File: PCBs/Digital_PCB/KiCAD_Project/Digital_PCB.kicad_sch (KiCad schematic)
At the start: 46 parts, among them J1 NP_Conn_01x02_Relief, J2 Board to Board, J3 NP_Conn_01x04_Relief, J4 1-0001205, J5 NP_Conn_01x04, J6 NP_Conn_01x02_Relief, J7 NP_Conn_01x04, U1 1-0000207, Y1 1-0000721

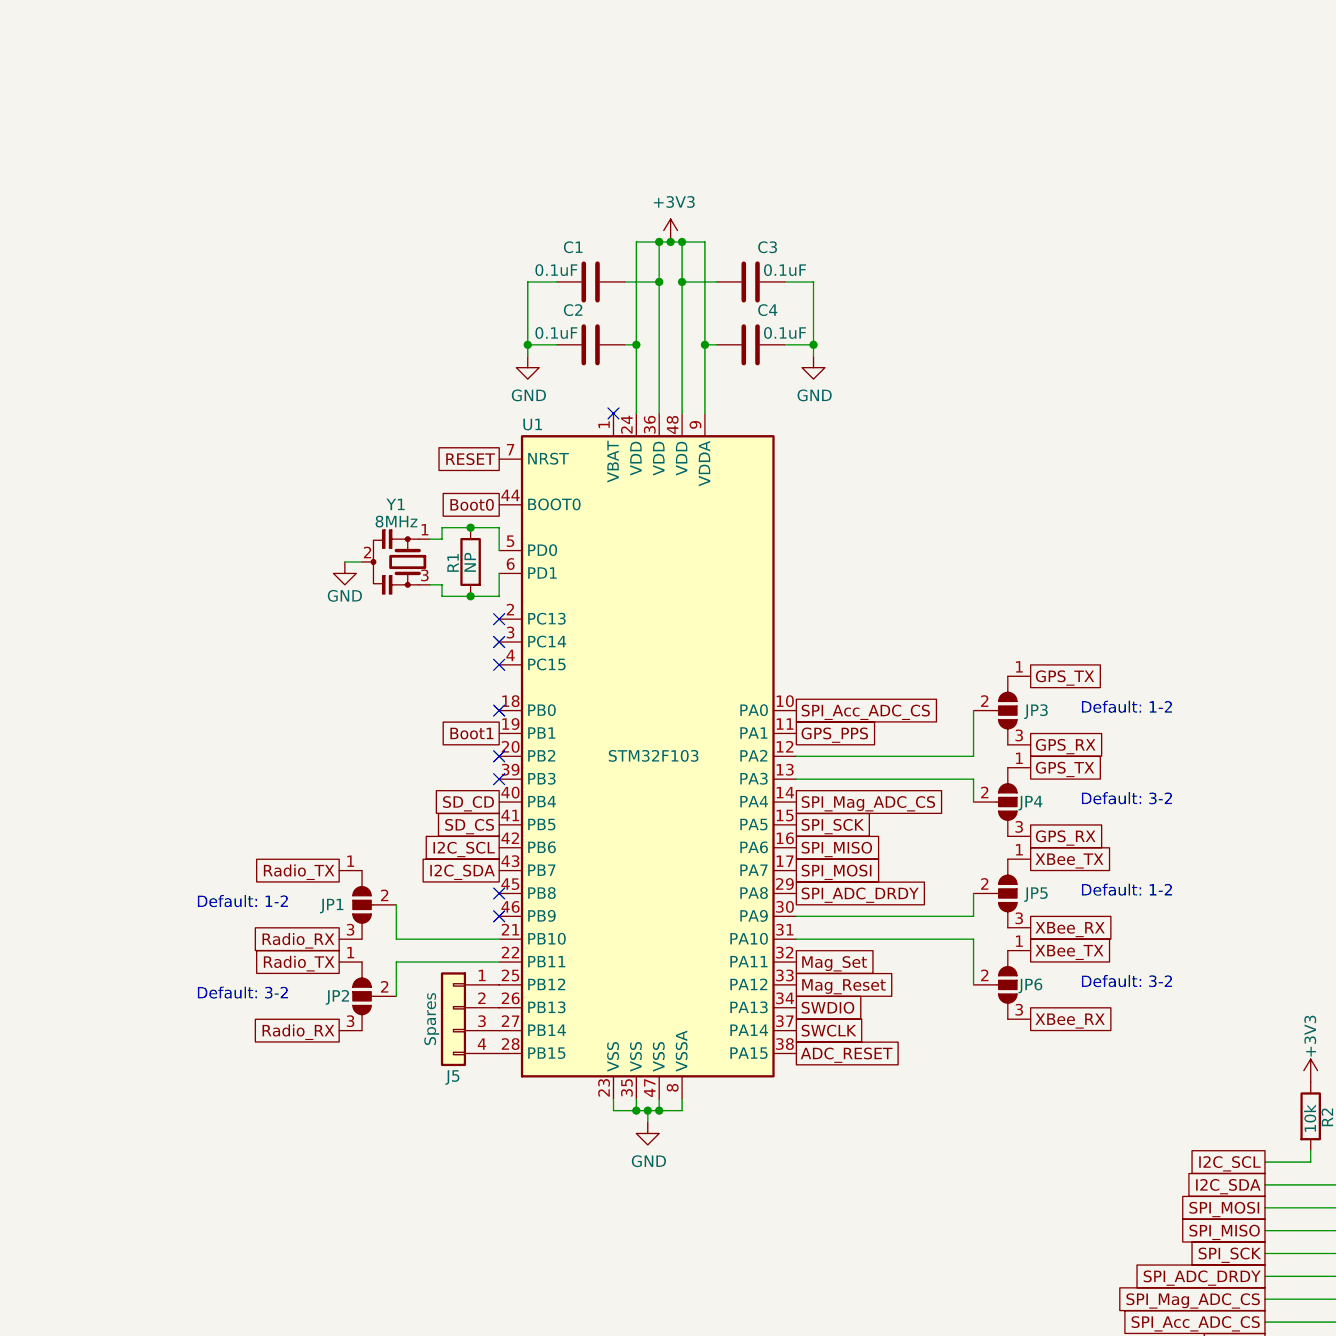
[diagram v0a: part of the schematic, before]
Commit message: Digital PCB Revisions: Fixed ERC Footprint/Symbol Errors Fixed Remaining ERC Errors Relocated U7 to bottom of PCB
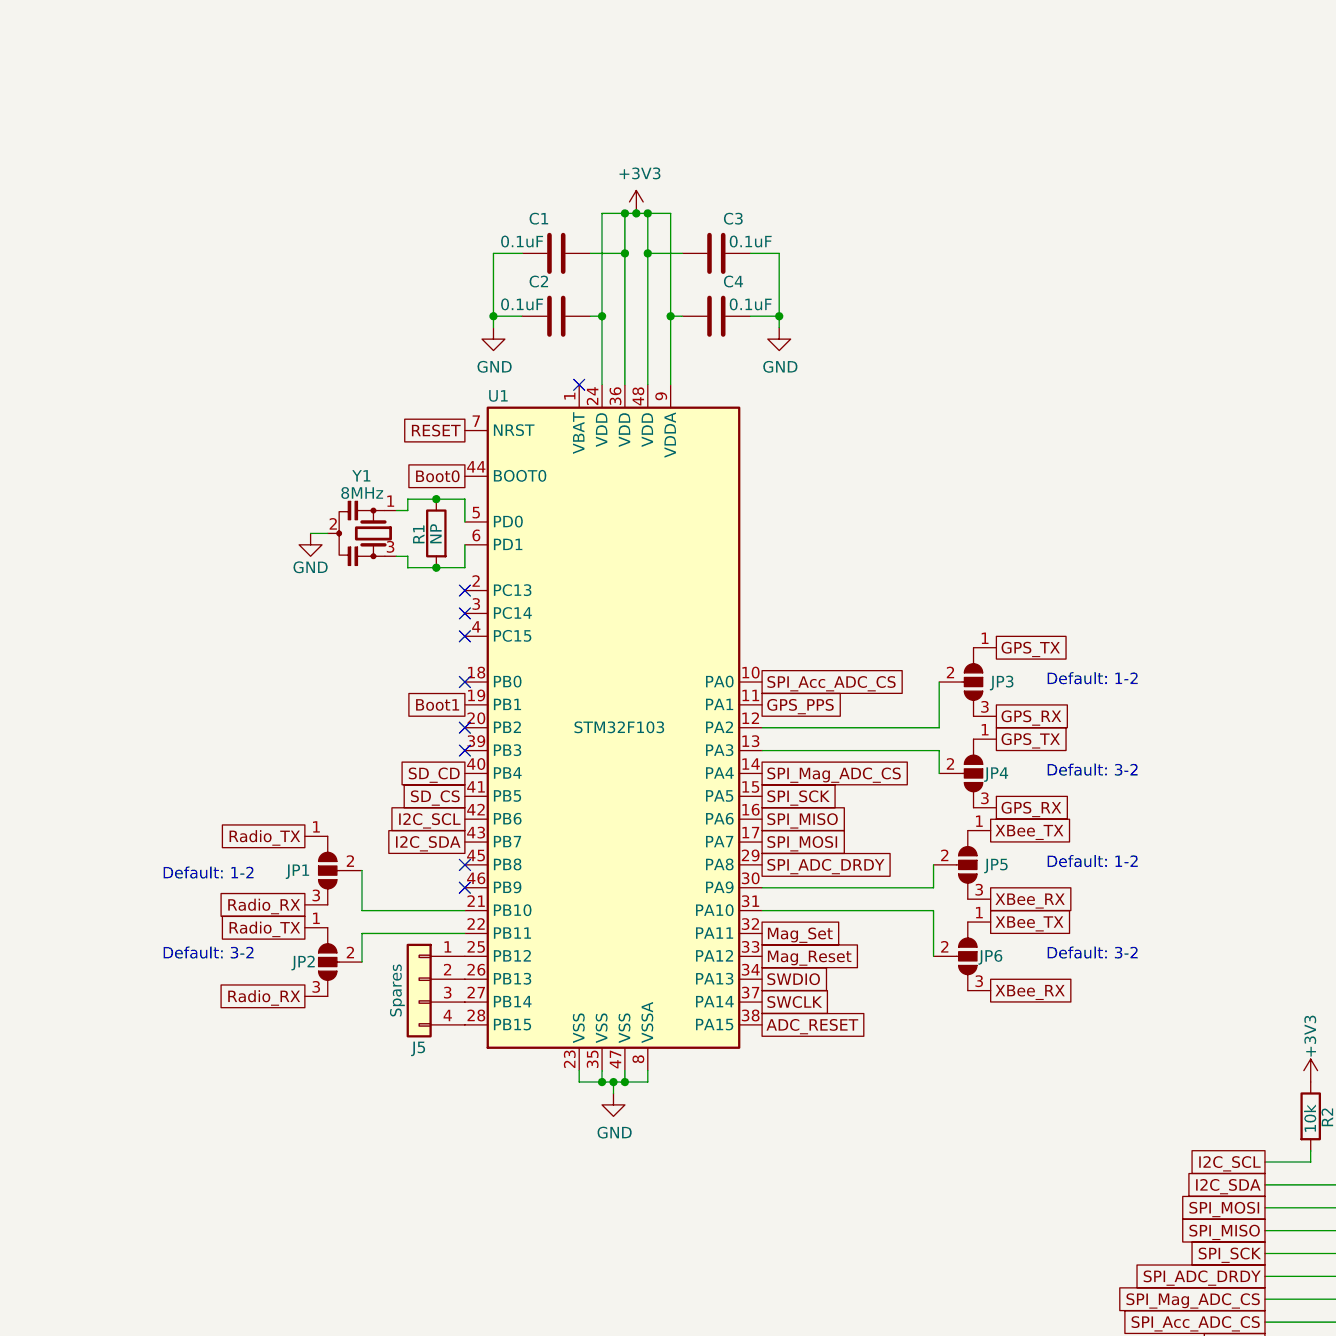
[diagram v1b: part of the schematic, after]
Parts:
- JP1, JP2, JP3, JP4, JP5, JP6: now left out of the parts list
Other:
- moved on the sheet: C1, C2, C3, C4, J5, JP3, JP4, R1, U1, Y1
